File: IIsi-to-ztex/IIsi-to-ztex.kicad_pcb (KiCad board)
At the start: 4 copper layers, 118 x 100 mm, 58 parts, among them J1 Conn_02x07_Odd_Even, J2 650906-5, J3 10029449-111RLF (HDMI A), J4 A2541HWR-2x6P (Pmod 2x6 F R), SW1 SW_SPDT, U1 SN74CB3T3245PWR, U10 SN74CB3T3245PWR, U11 SN74CB3T3245PWR, U12 TPD12S016PWR, U13 SN74CB3T3245PWR, U2 SN74CB3T3245PWR, U3 SN74CB3T3245PWR, U4 SN74CB3T3245PWR, U5 SN74CB3T3245PWR, U6 SN74CB3T3245PWR, U7 SN74CB3T3245PWR, U8 SN74CB3T3245PWR, U9 SN74CB3T3245PWR

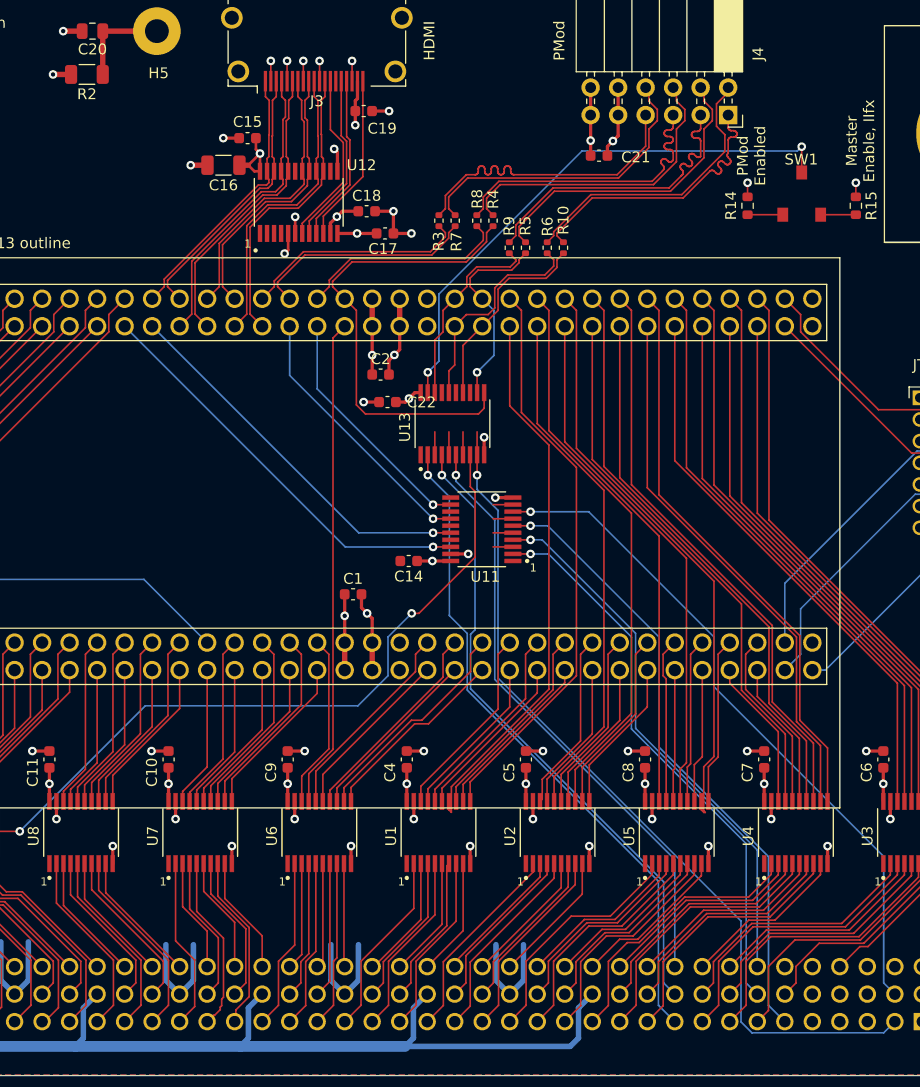
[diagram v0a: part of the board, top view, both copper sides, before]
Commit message: rework /HALT
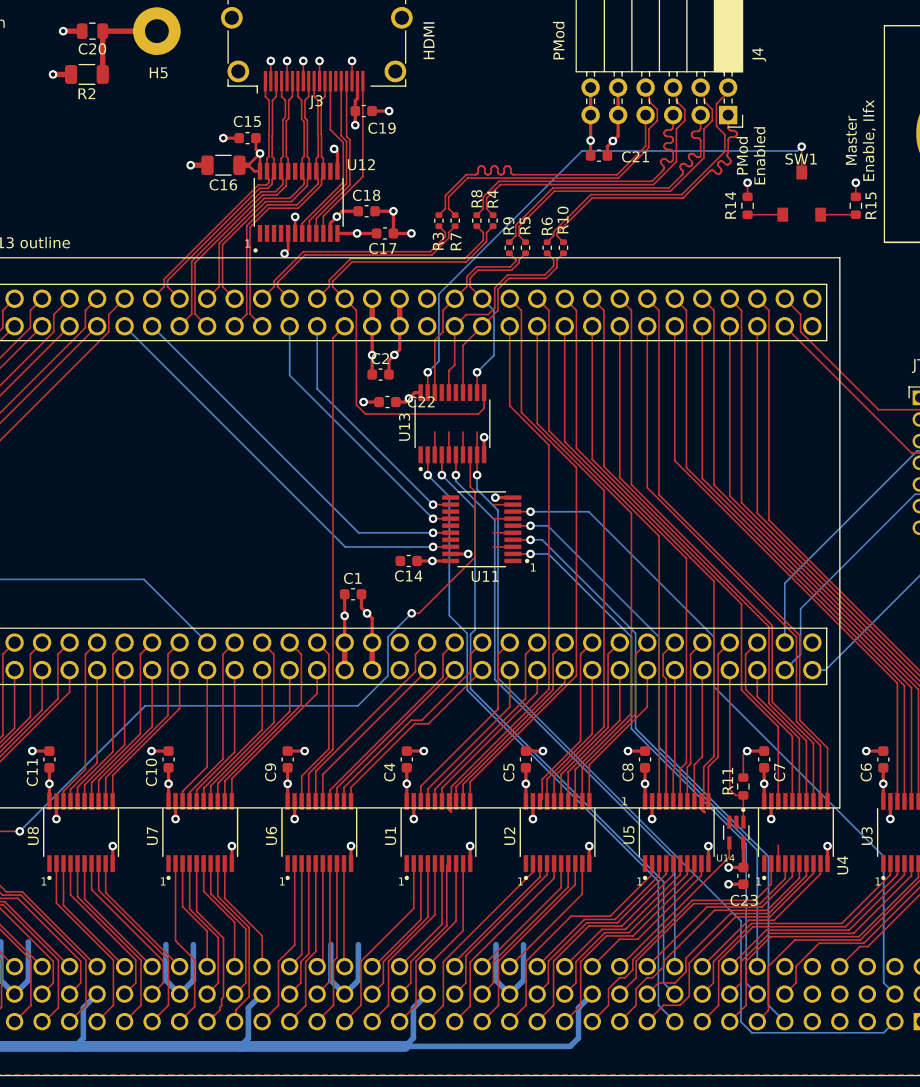
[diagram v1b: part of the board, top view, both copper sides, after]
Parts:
- added C23: 100nF, Capacitor_SMD:C_0603_1608Metric, F.Cu at (187.6, 134.0)
- added R11: 10k, Resistor_SMD:R_0603_1608Metric, F.Cu at (187.6, 125.8)
- added U14: SN74LV1T125DCKR, For_SeeedStudio:SOT65P210X110-5N, F.Cu at (187.0, 130.0)
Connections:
- JAB1 pad 57: D0_3V3 -> ~HALT_3V3
- JAB1 pad 59: ~RESET_3V3 -> FC0_3V3
- JCD1 pad 48: ~HALT_3V3 -> D0_3V3
- JCD1 pad 49: FC0_3V3 -> ~RESET_3V3
- U4 pad 14: FC0_3V3 -> ~RESET_3V3
- U4 pad 15: ~RESET_3V3 -> FC0_3V3
- U4 pad 17: ~HALT_3V3 -> Net-(U4-Pad17)
- U4 pad 3: ~HALT -> GND
- U4 pad 5: ~RESET -> FC0
- U4 pad 6: FC0 -> ~RESET
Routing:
- net D0_3V3: track 14.0 -> 53.5 mm
- net ~HALT_3V3: track 53.8 -> 15.0 mm
- net ~RESET_3V3: track 13.7 -> 51.0 mm
- net FC0_3V3: track 51.0 -> 13.7 mm
- net GND: track 475.8 -> 481.4 mm, vias 53 -> 54
- net +3V3: track 160.7 -> 164.4 mm, vias 20 -> 21
- net ~HALT: track 19.2 -> 15.6 mm
- net FC2: track 24.3 -> 23.7 mm
- net FC0: track 18.6 -> 18.0 mm

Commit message: cleanup DRC
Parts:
- removed SW1: SW_SPDT, For_SeeedStudio:CJS-1201B
- added C24: 100nF, Capacitor_SMD:C_0603_1608Metric, F.Cu at (141.8, 63.9)
- added S1: SSAJ110100, For_SeeedStudio:SW_SSAJ110100, F.Cu at (195.0, 54.5)
- moved R14 14.9 mm to (194.0, 58.5), turned to 90 degrees
- moved R15 13.8 mm to (196.0, 58.5), turned to 90 degrees
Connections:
- U13 pad 13: Net-(U13-Pad13) -> PMOD-56+
- U13 pad 17: Net-(U13-Pad17) -> PMOD-56-
- U13 pad 3: GND -> ~IRQ2
- U13 pad 7: GND -> ~IRQ3
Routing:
- net ~IRQ3: track 0.00 -> 72.6 mm, vias 0 -> 1
- net ~IRQ2: track 0.00 -> 72.2 mm, vias 0 -> 1
- net PMOD-56+: track 20.8 -> 46.3 mm, vias 0 -> 1
- net PMOD-56-: track 20.8 -> 40.7 mm, vias 0 -> 1
- net HDMI_CLK-: track 27.7 -> 44.5 mm
- net HDMI_D0-: track 25.6 -> 42.2 mm
- net +5V: track 183.8 -> 200.1 mm, vias 3 -> 5
- net HDMI_CLK+: track 27.7 -> 43.8 mm
- net HDMI_D0+: track 25.6 -> 37.3 mm
- net HDMI_D2-: track 25.3 -> 36.5 mm
- net ~MASTER_OE: track 51.0 -> 61.2 mm
- net CACHE: track 63.3 -> 69.8 mm
- net GND: track 481.4 -> 487.7 mm, vias 54 -> 56
- net HDMI_D1-: track 27.7 -> 32.6 mm
- net HDMI_D2+: track 25.3 -> 30.1 mm
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
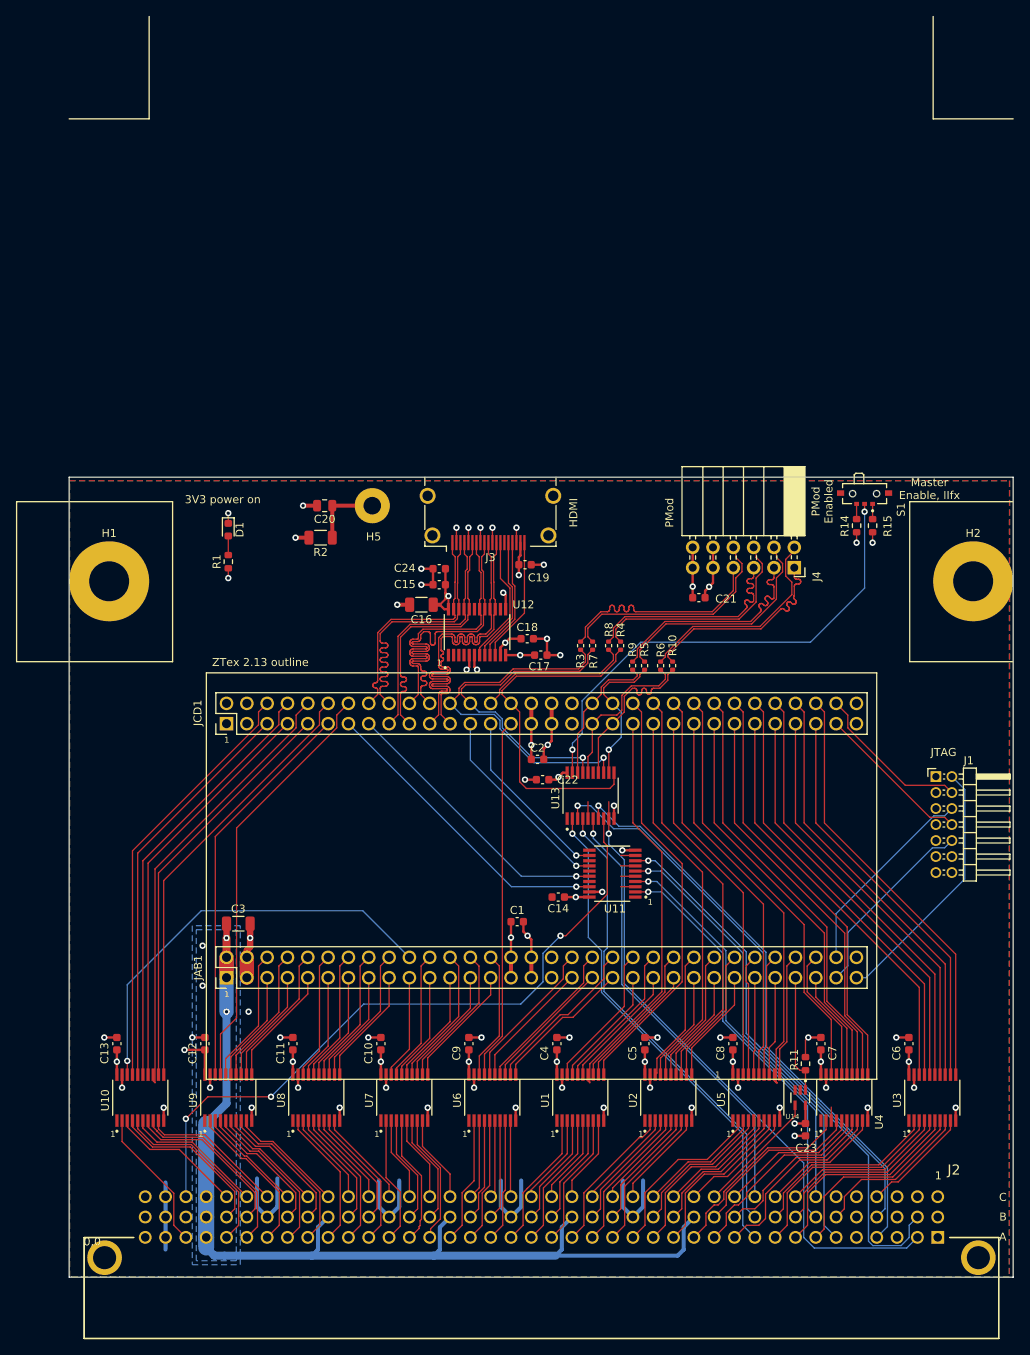
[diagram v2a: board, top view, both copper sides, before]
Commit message: connect rbv to last pmod pin
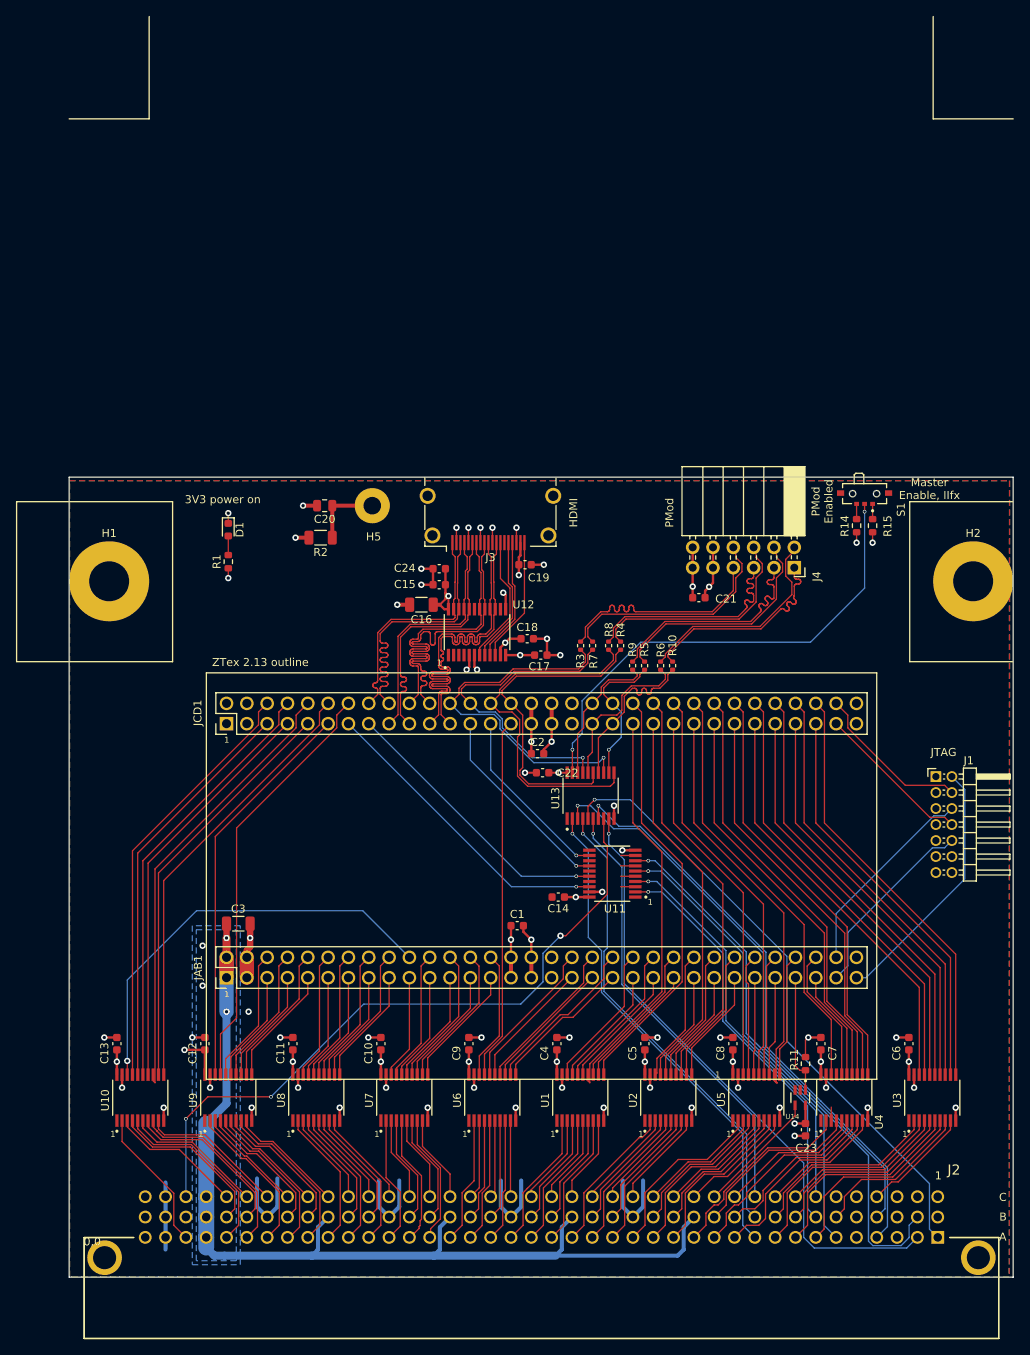
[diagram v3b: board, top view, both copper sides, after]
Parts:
- moved C22 0.87 mm to (154.8, 89.4)
- moved C2 0.71 mm to (154.1, 87.0)
- moved C1 0.50 mm to (151.6, 108.5)
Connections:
- U13 pad 11: PMOD-78- -> PMOD-78+
- U13 pad 15: Net-(U13-Pad15) -> PMOD-78-
- U13 pad 5: GND -> ~RBV
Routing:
- net ~RBV: track 0.00 -> 77.8 mm, vias 0 -> 1
- net PMOD-78+: track 19.5 -> 45.1 mm
- net PMOD-78-: track 43.5 -> 40.1 mm
- net GND: track 487.7 -> 484.4 mm
- net ~FPU: track 79.9 -> 77.8 mm
- net +3V3: track 167.1 -> 165.5 mm
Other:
- net class Default: via_dia 0.8 -> 0.45; via_drill 0.4 -> 0.3
- net class PWR added: clearance 0.1524, trace_width 0.2, via_dia 0.8, via_drill 0.4

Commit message: some rerouting
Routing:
- net CACHE: track 69.8 -> 62.0 mm
- net ~FPU: track 77.8 -> 75.5 mm
- net ~IRQ2: track 72.2 -> 70.1 mm
- net ~RBV: track 77.8 -> 78.4 mm
- net +3V3: track 165.5 -> 166.0 mm

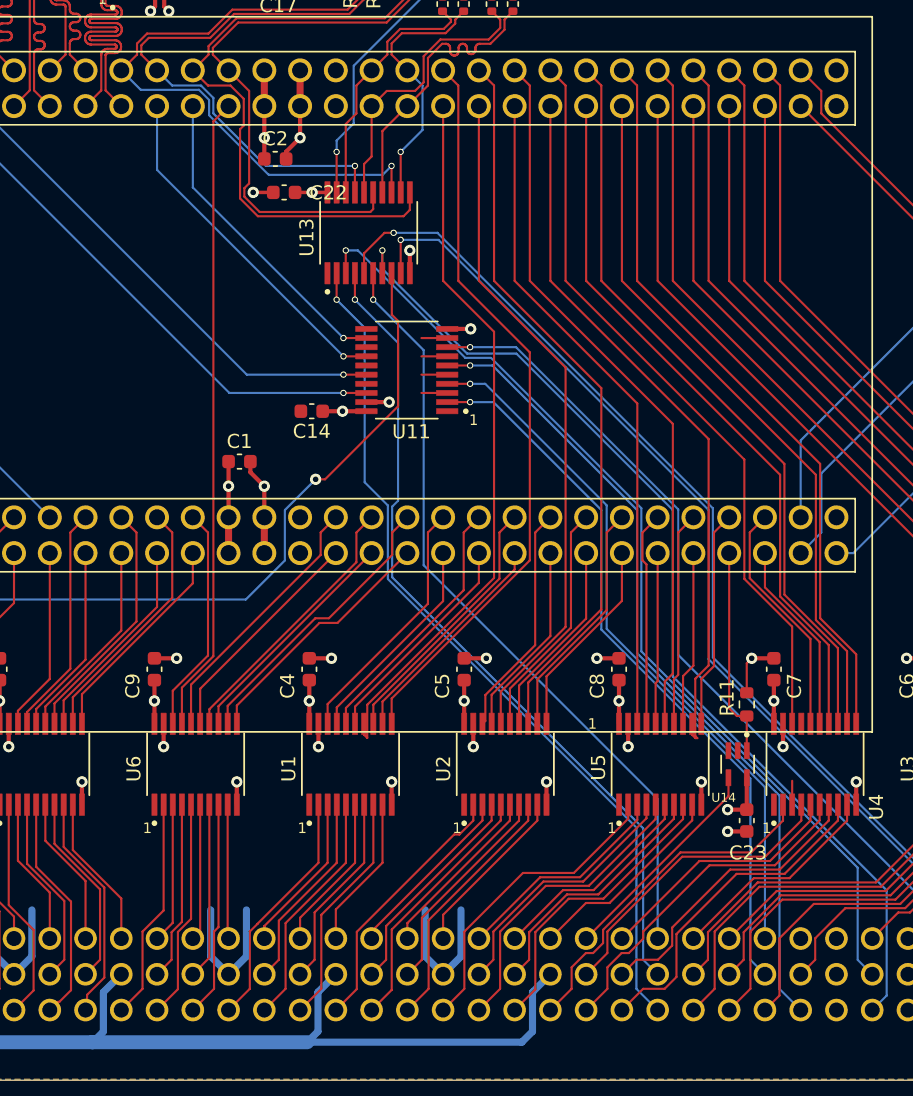
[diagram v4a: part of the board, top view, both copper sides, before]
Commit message: some pull-(up,down)s
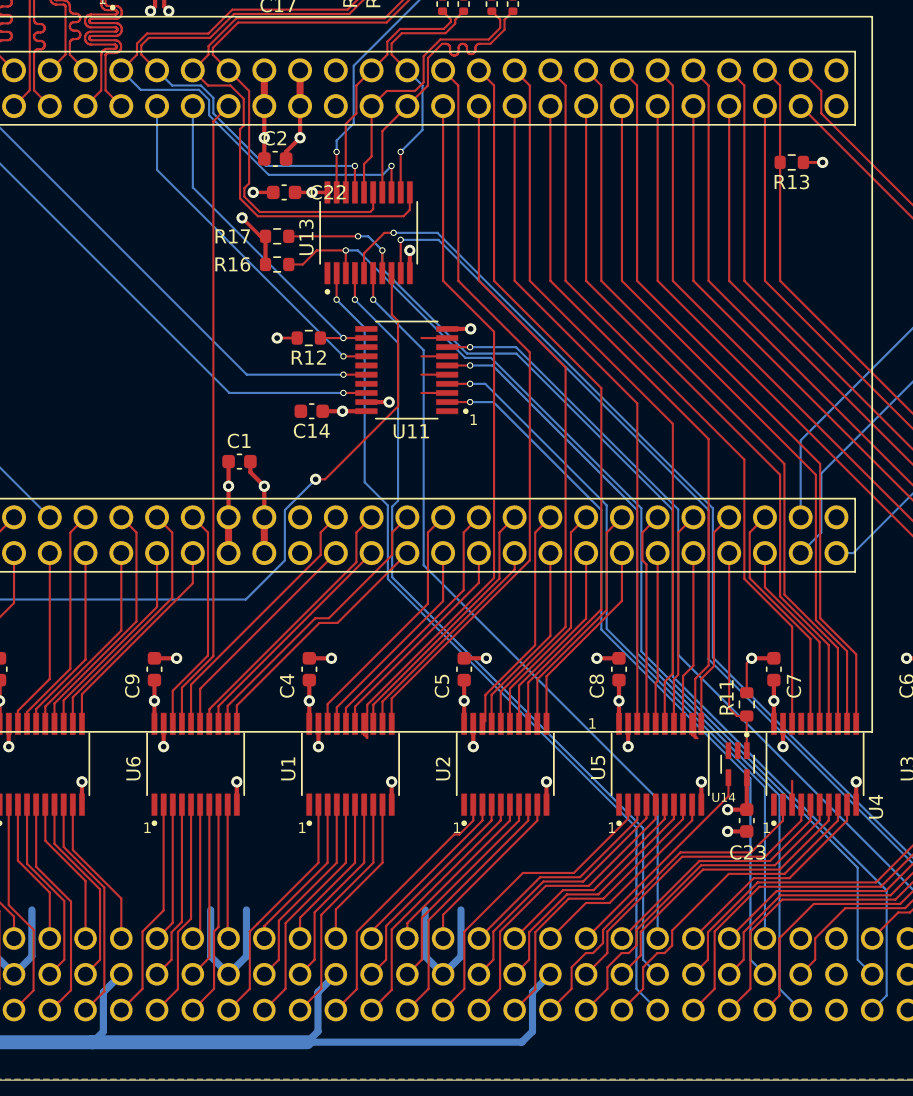
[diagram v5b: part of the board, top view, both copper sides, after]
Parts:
- added R12: 10k, Resistor_SMD:R_0603_1608Metric, F.Cu at (156.5, 99.7)
- added R13: 10k, Resistor_SMD:R_0603_1608Metric, F.Cu at (190.8, 87.2)
- added R16: 10k, Resistor_SMD:R_0603_1608Metric, F.Cu at (154.2, 94.5)
- added R17: 10k, Resistor_SMD:R_0603_1608Metric, F.Cu at (154.2, 92.5)
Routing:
- net +5V: track 200.1 -> 210.8 mm, vias 5 -> 6
- net ~IRQ3: track 72.9 -> 80.0 mm, vias 1 -> 2
- net ~IRQ2: track 70.1 -> 74.6 mm
- net CACHE_3V3: track 22.5 -> 24.2 mm
- net GND: track 484.5 -> 485.9 mm, vias 56 -> 57
- net +3V3: track 166.0 -> 167.4 mm, vias 21 -> 22

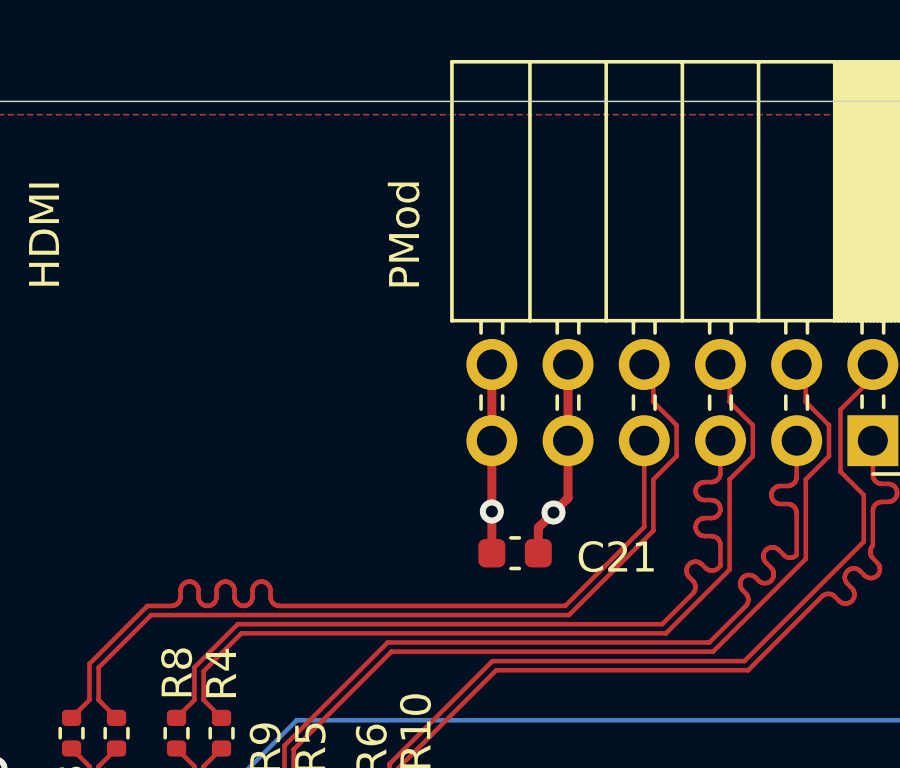
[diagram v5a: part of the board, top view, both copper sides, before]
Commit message: pmod orientation
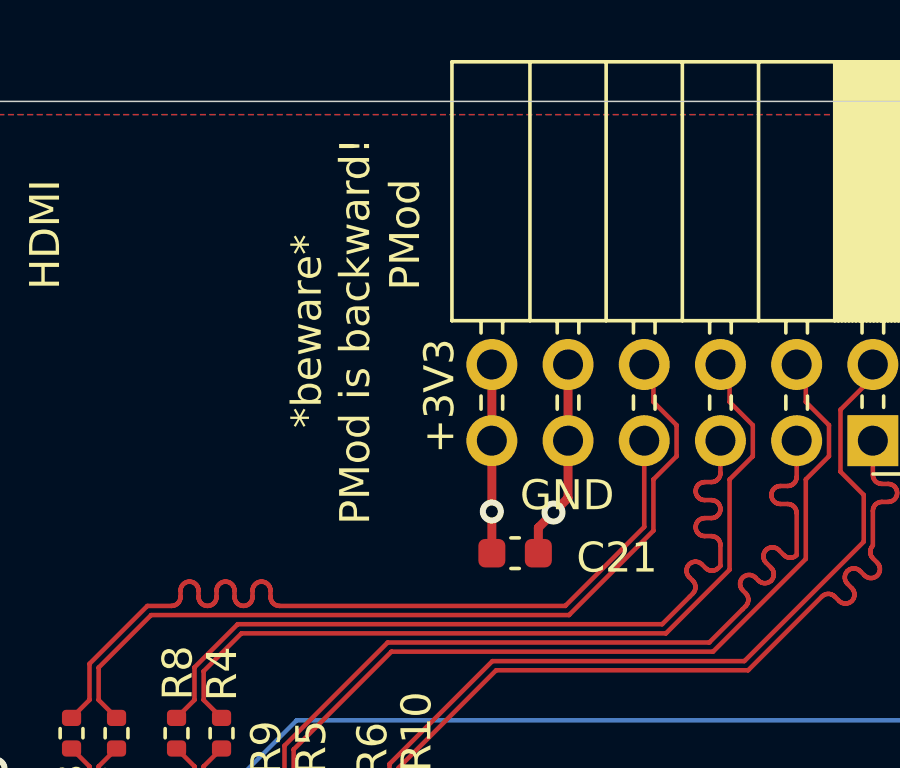
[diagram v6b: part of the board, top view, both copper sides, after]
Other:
- board text added: "*beware* PMod is backward!"
- board text added: "+3V3"
- board text added: "GND"
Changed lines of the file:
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@@
   (general
     (thickness 1.6)
-    (drawings 82)
+    (drawings 86)
     (tracks 2949)
     (zones 0)
@@
     )
   )
+  (dimension 24.74 (width 0.15) (layer Dwgs.User)
+    (gr_text "24.740 mm" (at 79.26 140.07 90) (layer Dwgs.User)
+      (effects (font (size 1 1) (thickness 0.15)))
+    )
+    (feature1 (pts (xy 95.57 127.7) (xy 79.973579 127.7)))
+    (feature2 (pts (xy 95.57 152.44) (xy 79.973579 152.44)))
+    (crossbar (pts (xy 80.56 152.44) (xy 80.56 127.7)))
+    (arrow1a (pts (xy 80.56 127.7) (xy 81.146421 128.826504)))
+    (arrow1b (pts (xy 80.56 127.7) (xy 79.973579 128.826504)))
+    (arrow2a (pts (xy 80.56 152.44) (xy 81.146421 151.313496)))
+    (arrow2b (pts (xy 80.56 152.44) (xy 79.973579 151.313496)))
+  )
+  (gr_text "*beware*\nPMod is backward!" (at 168.15 60.1 90) (layer F.SilkS)
+    (effects (font (size 1 1) (thickness 0.15)))
+  )
+  (gr_text GND (at 176.02 65.57) (layer F.SilkS)
+    (effects (font (size 1 1) (thickness 0.15)))
+  )
+  (gr_text +3V3 (at 171.76 62.26 90) (layer F.SilkS)
+    (effects (font (size 1 1) (thickness 0.15)))
+  )
   (dimension 31.75 (width 0.15) (layer Dwgs.User)
